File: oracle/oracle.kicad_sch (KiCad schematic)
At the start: 20 parts, among them J10 EXT_PF5, J6 EXT_AREF, J9 EXT_PE6, U1 ATmega32U4-A, U2 WeMos_D1_mini, Y1 16MHz

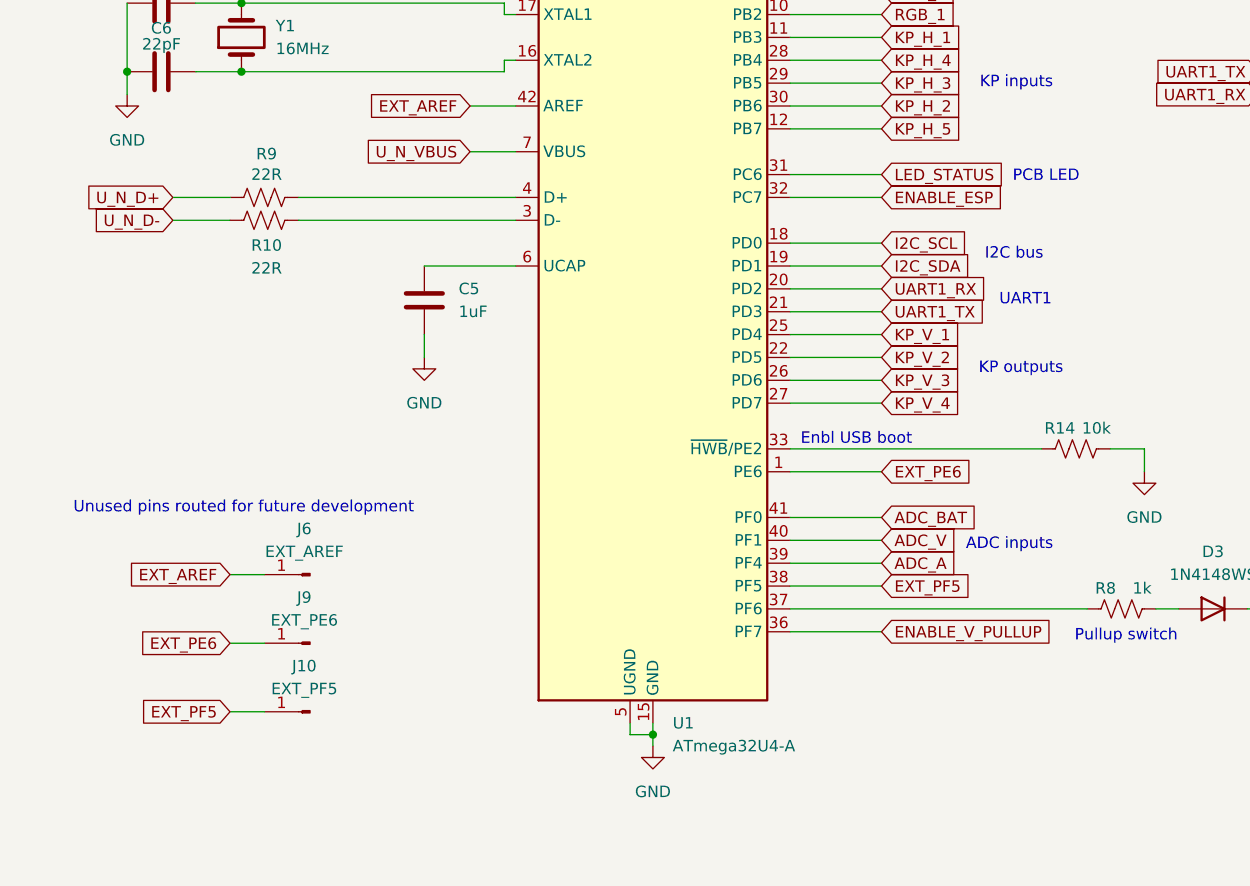
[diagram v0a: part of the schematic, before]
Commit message: add n_core firmware add e_core firmware stub update PCB
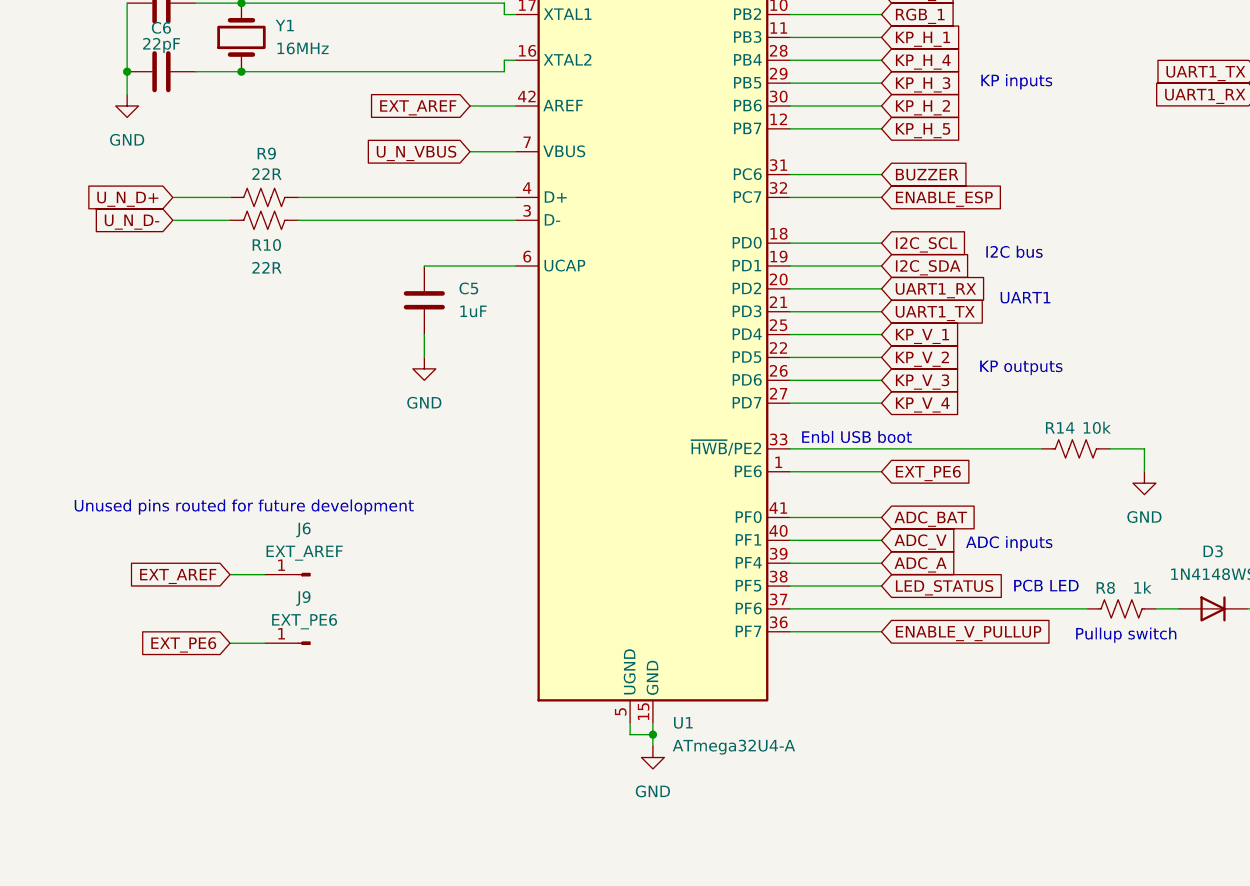
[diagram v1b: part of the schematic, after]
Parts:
- removed J10: EXT_PF5, Connector_PinSocket_2.54mm:PinSocket_1x01_P2.54mm_Vertical, symbol Connector:Conn_01x01_Pin
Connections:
- net EXT_PF5 is gone; now on net LED_STATUS: U1.38 (PF5)
- net LED_STATUS: no longer U1.31 (PC6)
- new net BUZZER: U1.31 (PC6)
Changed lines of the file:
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@@
 	(wire
 		(pts
+			(xy 116.84 134.62) (xy 127 134.62)
+		)
+		(stroke
+			(width 0)
+			(type default)
+		)
+	)
+	(wire
+		(pts
 			(xy 99.06 151.13) (xy 101.6 151.13)
 		)
@@
 	(wire
 		(pts
-			(xy 116.84 134.62) (xy 127 134.62)
-		)
-		(stroke
-			(width 0)
-			(type default)
-		)
-	)
-	(wire
-		(pts
 			(xy 116.84 66.04) (xy 127 66.04)
 		)
@@
 	(wire
 		(pts
-			(xy 116.84 88.9) (xy 127 88.9)
-		)
-		(stroke
-			(width 0)
-			(type default)
-		)
-	)
-	(wire
-		(pts
 			(xy 240.03 77.47) (xy 245.11 77.47)
 		)
@@
 	(wire
 		(pts
-			(xy 54.61 148.59) (xy 58.42 148.59)
-		)
-		(stroke
-			(width 0)
-			(type default)
-		)
-	)
-	(wire
-		(pts
 			(xy 62.23 93.98) (xy 86.36 93.98)
 		)
@@
 	(wire
 		(pts
+			(xy 116.84 88.9) (xy 127 88.9)
+		)
+		(stroke
+			(width 0)
+			(type default)
+		)
+	)
+	(wire
+		(pts
 			(xy 229.87 46.99) (xy 227.33 46.99)
 		)
@@
 	(text "PCB LED"
 		(exclude_from_sim no)
-		(at 145.288 89.154 0)
+		(at 145.288 134.874 0)
 		(effects
 			(font
@@
 		)
 	)
-	(global_label "EXT_PF5"
-		(shape input)
-		(at 54.61 148.59 180)
-		(fields_autoplaced yes)
-		(effects
-			(font
-				(size 1.27 1.27)
-			)
-			(justify right)
-		)
-		(property "Intersheetrefs" "${INTERSHEET_REFS}"
-			(at 43.763 148.59 0)
-			(effects
-				(font
-					(size 1.27 1.27)
-				)
-				(justify right)
-				(hide yes)
-			)
-		)
-	)
 	(global_label "KP_H_5"
 		(shape input)
@@
 		)
 	)
-	(global_label "EXT_PF5"
+	(global_label "BUZZER"
 		(shape input)
-		(at 127 134.62 0)
+		(at 127 88.9 0)
 		(fields_autoplaced yes)
 		(effects
@@
 		)
 		(property "Intersheetrefs" "${INTERSHEET_REFS}"
-			(at 137.847 134.62 0)
+			(at 137.4237 88.9 0)
 			(effects
 				(font
@@
 	(global_label "LED_STATUS"
 		(shape input)
-		(at 127 88.9 0)
+		(at 127 134.62 0)
 		(fields_autoplaced yes)
 		(effects
@@
 		)
 		(property "Intersheetrefs" "${INTERSHEET_REFS}"
-			(at 141.1732 88.9 0)
+			(at 141.1732 134.62 0)
 			(effects
 				(font
@@
 					(unit 1)
 				)
-			)
-		)
-	)
-	(symbol
-		(lib_id "Connector:Conn_01x01_Pin")
-		(at 63.5 148.59 180)
-		(unit 1)
-		(exclude_from_sim no)
-		(in_bom yes)
-		(on_board yes)
-		(dnp no)
-		(fields_autoplaced yes)
-		(property "Reference" "J10"
-			(at 62.865 143.51 0)
-			(effects
-				(font
-					(size 1.27 1.27)
-				)
-			)
-		)
-		(property "Value" "EXT_PF5"
-			(at 62.865 146.05 0)
-			(effects
-				(font
-					(size 1.27 1.27)
-				)
-			)
-		)
-		(property "Footprint" "Connector_PinSocket_2.54mm:PinSocket_1x01_P2.54mm_Vertical"
-			(at 63.5 148.59 0)
-			(effects
-				(font
-					(size 1.27 1.27)
-				)
-				(hide yes)
-			)
-		)
-		(property "Datasheet" "~"
-			(at 63.5 148.59 0)
-			(effects
-				(font
-					(size 1.27 1.27)
-				)
-				(hide yes)
-			)
-		)
-		(property "Description" "Generic connector, single row, 01x01, script generated"
-			(at 63.5 148.59 0)
-			(effects
-				(font
-					(size 1.27 1.27)
-				)
-				(hide yes)
-			)
-		)
-		(pin "1"
-		)
-		(instances
-			(project "oracle"
-				(path "/45530167-148b-49af-a925-e406b597863f"
-					(reference "J10")
-					(unit 1)
-				)
